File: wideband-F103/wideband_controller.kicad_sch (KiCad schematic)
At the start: 109 parts, among them J1 FTSH-107-01-F-DV-K, J2 Conn_02x06_Top_Bottom, J3 Conn_02x02_Odd_Even, J4 Conn_01x10, Q2 BTS3028, U1 MCP6004, U2 STM32F103C6Tx, U3 GS8332, U4 LM78M05_TO252, U5 XC6206P332MR, U6 REF3033, U7 MCP6002T-I/SN, U8 TJA1051T-3

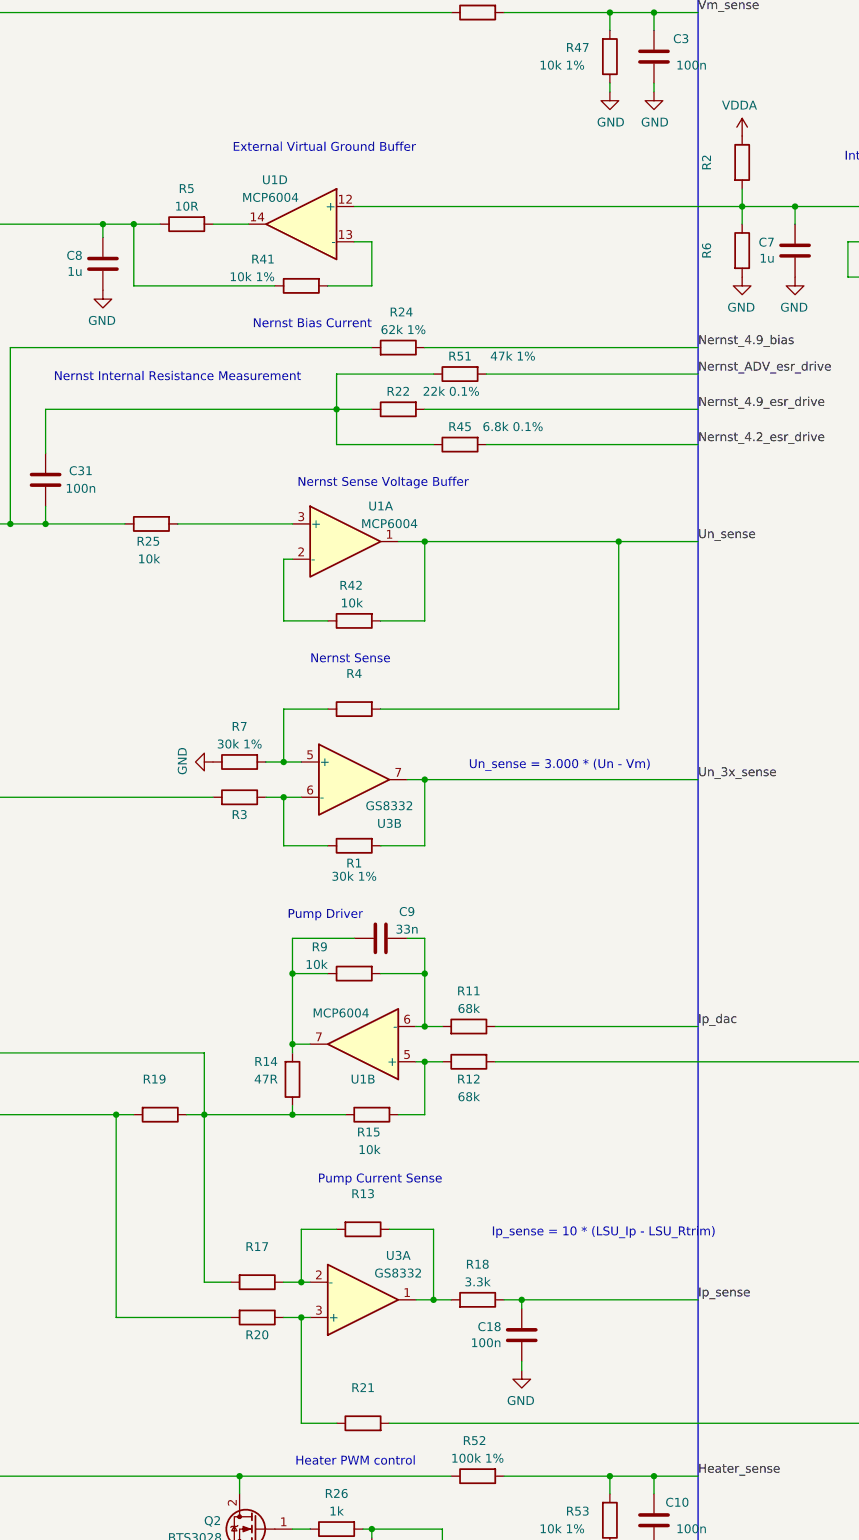
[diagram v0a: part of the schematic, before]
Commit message: Fix LCSC for few components
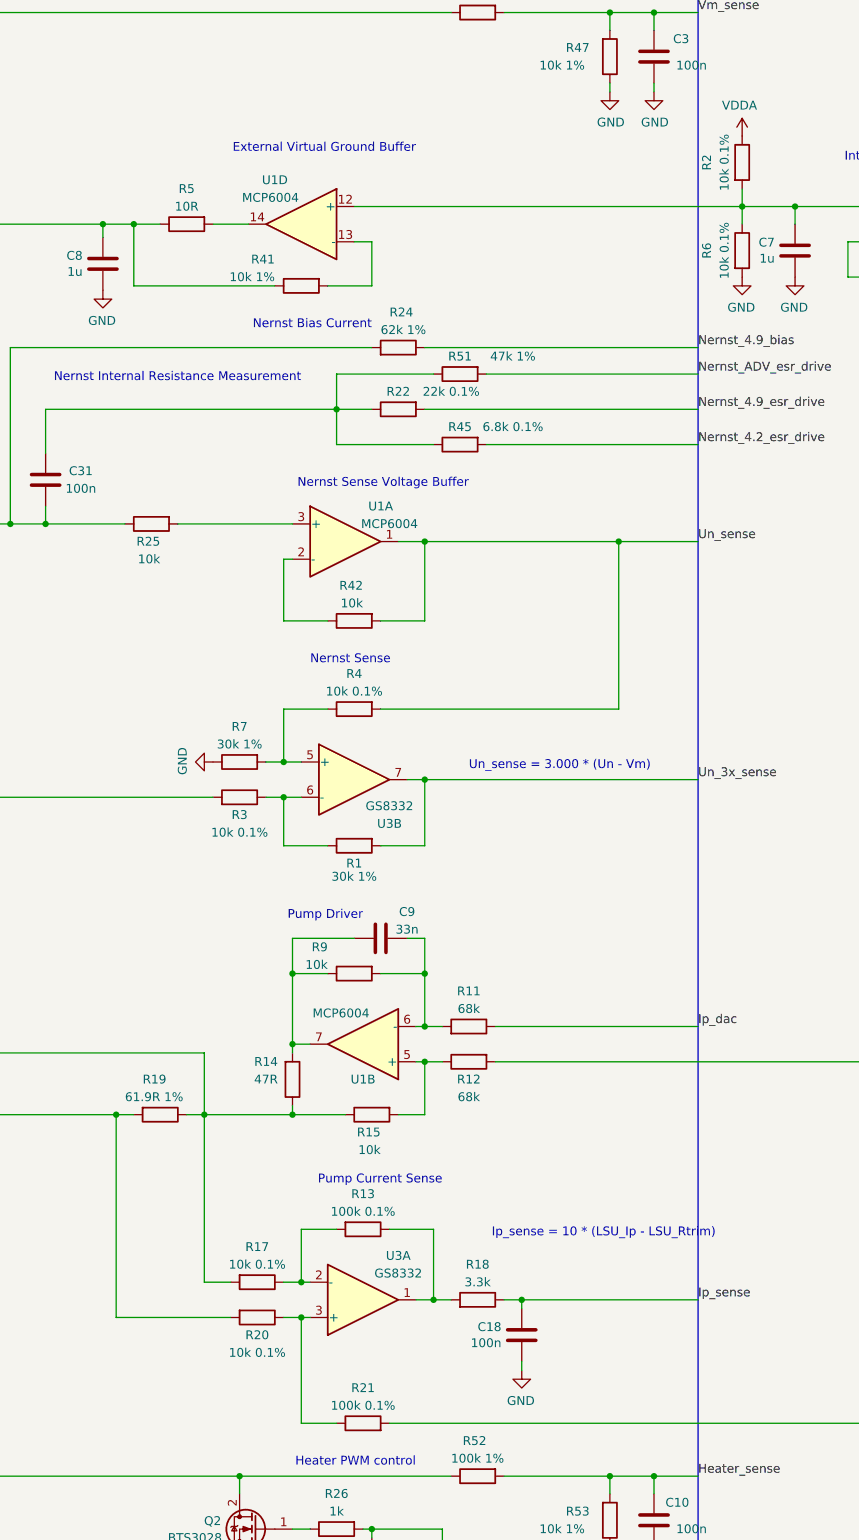
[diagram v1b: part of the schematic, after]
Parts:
- D6: LCSC C2128 -> C81598
- R1, R7: LCSC C25776 -> C22984
- R13, R21: value (none) -> 100k 0.1%; footprint (none) -> Resistor_SMD:R_0603_1608Metric; LCSC C328415 -> C122538
- R17, R2, R20, R3, R4, R6: value (none) -> 10k 0.1%; footprint (none) -> Resistor_SMD:R_0603_1608Metric
- R19: value (none) -> 61.9R 1%; footprint (none) -> Resistor_SMD:R_0805_2012Metric
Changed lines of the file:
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@@
       (effects (font (size 1.27 1.27)) hide)
     )
-    (property "LCSC" "C25776" (id 4) (at 185.42 182.245 0)
+    (property "LCSC" "C22984" (id 4) (at 185.42 182.245 0)
       (effects (font (size 1.27 1.27)) hide)
     )
@@
     (in_bom yes) (on_board yes)
     (property "Reference" "R17" (id 0) (at 171.45 240.03 90))
-    (property "Value" "" (id 1) (at 171.45 242.57 90))
-    (property "Footprint" "" (id 2) (at 171.45 243.332 90)
+    (property "Value" "10k 0.1%" (id 1) (at 171.45 242.57 90))
+    (property "Footprint" "Resistor_SMD:R_0603_1608Metric" (id 2) (at 171.45 243.332 90)
       (effects (font (size 1.27 1.27)) hide)
     )
@@
     (in_bom yes) (on_board yes)
     (property "Reference" "R20" (id 0) (at 171.45 252.73 90))
-    (property "Value" "" (id 1) (at 171.45 255.27 90))
-    (property "Footprint" "" (id 2) (at 171.45 248.412 90)
+    (property "Value" "10k 0.1%" (id 1) (at 171.45 255.27 90))
+    (property "Footprint" "Resistor_SMD:R_0603_1608Metric" (id 2) (at 171.45 248.412 90)
       (effects (font (size 1.27 1.27)) hide)
     )
@@
       (effects (font (size 1.27 1.27)) (justify left))
     )
-    (property "Value" "" (id 1) (at 152.4 218.44 90)
+    (property "Value" "61.9R 1%" (id 1) (at 152.4 218.44 90)
       (effects (font (size 1.27 1.27)) (justify left))
     )
-    (property "Footprint" "" (id 2) (at 157.48 219.202 90)
+    (property "Footprint" "Resistor_SMD:R_0805_2012Metric" (id 2) (at 157.48 219.202 90)
       (effects (font (size 1.27 1.27)) hide)
     )
@@
     (in_bom yes) (on_board yes)
     (property "Reference" "R13" (id 0) (at 186.69 232.41 90))
-    (property "Value" "" (id 1) (at 186.69 234.95 90))
-    (property "Footprint" "" (id 2) (at 186.69 235.712 90)
+    (property "Value" "100k 0.1%" (id 1) (at 186.69 234.95 90))
+    (property "Footprint" "Resistor_SMD:R_0603_1608Metric" (id 2) (at 186.69 235.712 90)
       (effects (font (size 1.27 1.27)) hide)
     )
@@
       (effects (font (size 1.27 1.27)) hide)
     )
-    (property "LCSC" "C328415" (id 4) (at 186.69 237.49 0)
+    (property "LCSC" "C122538" (id 4) (at 186.69 237.49 0)
       (effects (font (size 1.27 1.27)) hide)
     )
@@
     (in_bom yes) (on_board yes)
     (property "Reference" "R21" (id 0) (at 186.69 260.35 90))
-    (property "Value" "" (id 1) (at 186.69 262.89 90))
-    (property "Footprint" "" (id 2) (at 186.69 267.208 90)
+    (property "Value" "100k 0.1%" (id 1) (at 186.69 262.89 90))
+    (property "Footprint" "Resistor_SMD:R_0603_1608Metric" (id 2) (at 186.69 267.208 90)
       (effects (font (size 1.27 1.27)) hide)
     )
@@
       (effects (font (size 1.27 1.27)) hide)
     )
-    (property "LCSC" "C328415" (id 4) (at 186.69 265.43 0)
+    (property "LCSC" "C122538" (id 4) (at 186.69 265.43 0)
       (effects (font (size 1.27 1.27)) hide)
     )
@@
     (in_bom yes) (on_board yes)
     (property "Reference" "R3" (id 0) (at 168.91 177.8 90))
-    (property "Value" "" (id 1) (at 168.91 180.34 90))
-    (property "Footprint" "" (id 2) (at 168.91 177.038 90)
+    (property "Value" "10k 0.1%" (id 1) (at 168.91 180.34 90))
+    (property "Footprint" "Resistor_SMD:R_0603_1608Metric" (id 2) (at 168.91 177.038 90)
       (effects (font (size 1.27 1.27)) hide)
     )
@@
     (in_bom yes) (on_board yes)
     (property "Reference" "R4" (id 0) (at 185.42 157.48 90))
-    (property "Value" "" (id 1) (at 185.42 160.02 90))
-    (property "Footprint" "" (id 2) (at 185.42 160.782 90)
+    (property "Value" "10k 0.1%" (id 1) (at 185.42 160.02 90))
+    (property "Footprint" "Resistor_SMD:R_0603_1608Metric" (id 2) (at 185.42 160.782 90)
       (effects (font (size 1.27 1.27)) hide)
     )
@@
       (effects (font (size 1.27 1.27)) hide)
     )
-    (property "LCSC" "C25776" (id 4) (at 168.91 170.18 0)
+    (property "LCSC" "C22984" (id 4) (at 168.91 170.18 0)
       (effects (font (size 1.27 1.27)) hide)
     )
@@
       (effects (font (size 1.27 1.27)) hide)
     )
-    (property "LCSC" "C2128" (id 4) (at 227.33 34.29 0)
+    (property "LCSC" "C81598" (id 4) (at 227.33 34.29 0)
       (effects (font (size 1.27 1.27)) hide)
     )
@@
     (in_bom yes) (on_board yes)
     (property "Reference" "R2" (id 0) (at 236.22 83.82 90))
-    (property "Value" "" (id 1) (at 238.76 83.82 90))
-    (property "Footprint" "" (id 2) (at 239.522 83.82 90)
+    (property "Value" "10k 0.1%" (id 1) (at 238.76 83.82 90))
+    (property "Footprint" "Resistor_SMD:R_0603_1608Metric" (id 2) (at 239.522 83.82 90)
       (effects (font (size 1.27 1.27)) hide)
     )
@@
     (in_bom yes) (on_board yes)
     (property "Reference" "R6" (id 0) (at 236.22 96.52 90))
-    (property "Value" "" (id 1) (at 238.76 96.52 90))
-    (property "Footprint" "" (id 2) (at 239.522 96.52 90)
+    (property "Value" "10k 0.1%" (id 1) (at 238.76 96.52 90))
+    (property "Footprint" "Resistor_SMD:R_0603_1608Metric" (id 2) (at 239.522 96.52 90)
       (effects (font (size 1.27 1.27)) hide)
     )
